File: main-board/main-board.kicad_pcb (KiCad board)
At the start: 4 copper layers, 142.9 x 86.4 mm, 168 parts, among them J1 BOOT, J10 8P8CDouble, J11 Qwiic, J12 Qwiic, J13 Qwiic, J14 EthernetLEDs, J2 USB Header, J3 JTAG, J4 5V Input, J5 StatusPanel, J6 Magjack, J7 8P8CDouble, J8 8P8CDouble, J9 8P8CDouble, Q1 N Channel, Q10 N Channel, Q11 N Channel, Q12 N Channel, Q13 P Channel, Q14 P Channel, Q15 P Channel, Q16 P Channel, Q17 P Channel, Q2 N Channel, Q3 N Channel, Q4 N Channel, Q5 P Channel, Q6 P Channel, Q7 P Channel, Q8 P Channel, Q9 N Channel, U1 STM32H743ZITx, U10 ISL83490, U11 ISL83490, U12 ISL83490, U13 W25Q80DVSNIG, U2 USBLC6-2SC6, U3 3.3V Reg, U4 KSZ8041MLL, U5 ISL83490, U6 ISL83490, U7 ISL83490, U8 ISL83490, U9 ISL83490, X1 20MHz Oscillator, X2 25MHz Oscillator

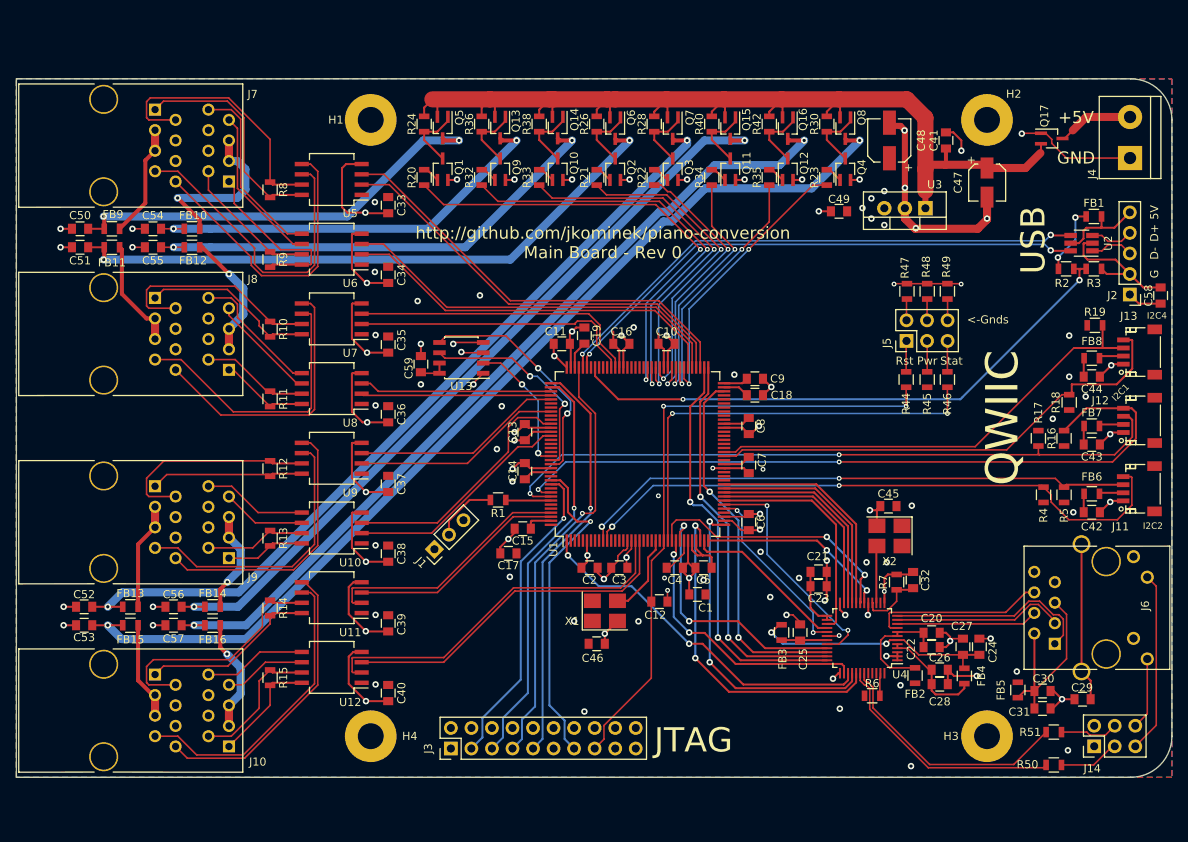
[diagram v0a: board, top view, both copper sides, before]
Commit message: First round of rev 1 changes. This was a complete relayout.
* RS485 transceiver footprint fixed
* Compressed board to 100x100mm exactly
* Removed ethernet
* Changed FET footprints to SOT-23
* Swapped USB D+/D- to correct positions
* Spaced out +5V and GND silkscreen on power input
* Added JLCPCB order number silkscreen
* Spaced out Qwiic headers
* Added some more space around 3.3V regulator.
* Slightly increased size of electrolytic caps.
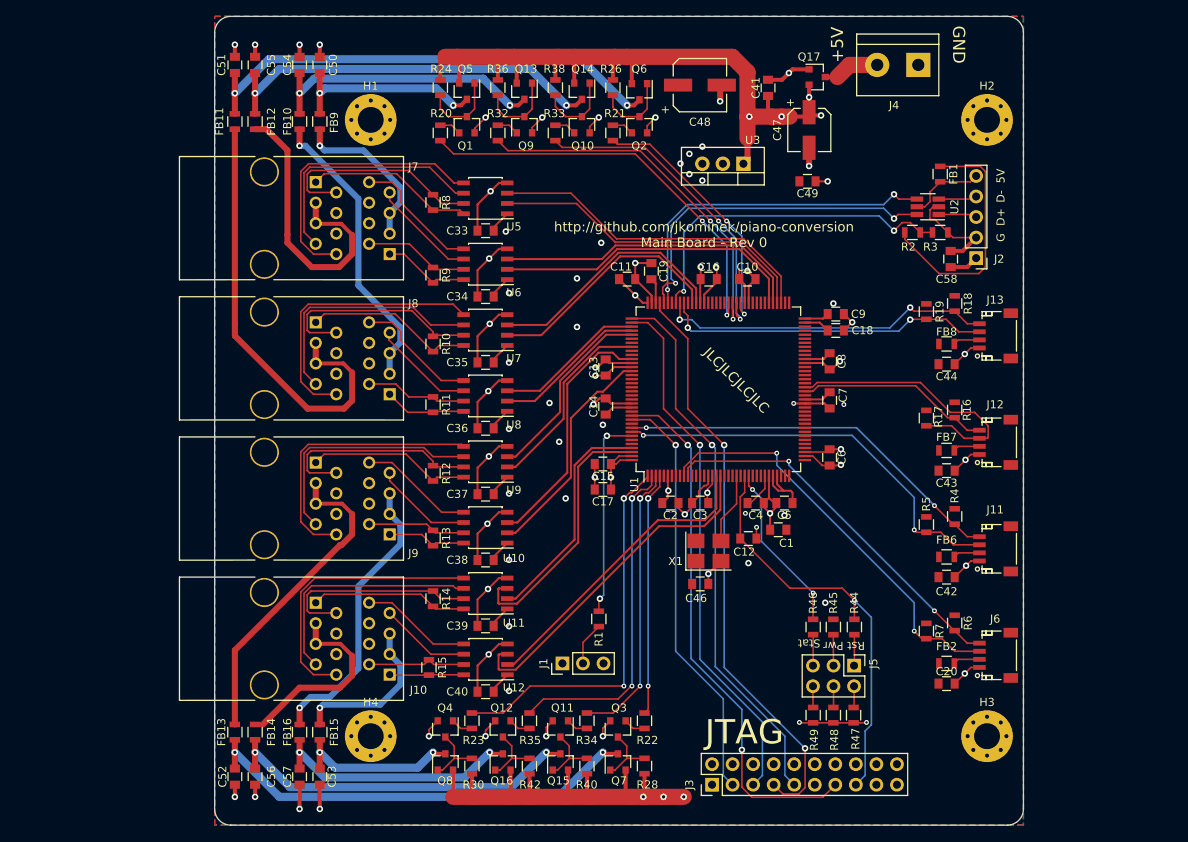
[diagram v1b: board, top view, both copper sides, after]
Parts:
- removed C21: 22uF, Capacitors_SMD:C_0805
- removed C22, C23, C25, C26, C27, C28, C29, C30, C31, C32: 0.1uF, Capacitors_SMD:C_0805
- removed C24: 1uF, Capacitors_SMD:C_0805
- removed C45: DC, Capacitors_SMD:C_0805
- removed C59: DC6, Capacitors_SMD:C_0805
- removed FB3, FB4, FB5: FB, Inductors_SMD:L_0805
- removed J14: EthernetLEDs, Pin_Headers:Pin_Header_Straight_2x03_Pitch2.54mm
- removed R50, R51: 330, Resistors_SMD:R_0805
- removed U13: W25Q80DVSNIG, Housings_SOIC:SOIC-8_3.9x4.9mm_Pitch1.27mm
- removed U4: KSZ8041MLL, Housings_QFP:LQFP-48_7x7mm_Pitch0.5mm
- removed X2: 25MHz Oscillator, Oscillators:Oscillator_SMD_SeikoEpson_SG8002CE-4pin_3.2x2.5mm_HandSoldering
- C20: value 22uF -> 1uF
- C47: footprint Capacitors_SMD:CP_Elec_4x4.5 -> Capacitors_SMD:CP_Elec_5x5.3
- C48: footprint Capacitors_SMD:CP_Elec_5x5.3 -> Capacitors_SMD:CP_Elec_6.3x5.8
- H1, H2, H3, H4: footprint Mounting_Holes:MountingHole_3.2mm_M3_Pad -> Mounting_Holes:MountingHole_3.2mm_M3_Pad_Via
- J6: value Magjack -> Qwiic; footprint footprints:J1B1211111CCD -> Connectors_JST:JST_SH_SM04B-SRSS-TB_04x1.00mm_Angled
- Q1, Q10, Q11, Q12, Q13, Q14, Q15, Q16, Q17, Q2, Q3, Q4, Q5, Q6, Q7, Q8, Q9: footprint TO_SOT_Packages_SMD:SOT-323_SC-70_Handsoldering -> TO_SOT_Packages_SMD:SOT-23
- R6: value 0 -> 1200
- R7: value 6490 -> 1200
- U10, U11, U12, U5, U6, U7, U8, U9: footprint Housings_SOIC:SO-8_5.3x6.2mm_Pitch1.27mm -> Housings_SOIC:SOIC-8_3.9x4.9mm_Pitch1.27mm
- moved Q8 92.7 mm to (123.5, 130.2), turned to 90 degrees
- moved R30 90.7 mm to (126.8, 130.7), turned to 90 degrees
- moved Q16 85.9 mm to (130.6, 130.2), turned to 90 degrees
- moved Q4 85.1 mm to (123.5, 126.1), turned to 270 degrees
- moved R42 84.7 mm to (133.9, 130.7), turned to 90 degrees
- moved Q15 81.1 mm to (137.8, 130.2), turned to 90 degrees
- moved R40 80.9 mm to (141.0, 130.7), turned to 90 degrees
- moved R23 80.2 mm to (126.8, 125.1), turned to 90 degrees
- moved R28 79.4 mm to (148.1, 130.7), turned to 90 degrees
- moved Q7 78.7 mm to (144.9, 130.2), turned to 90 degrees
- moved Q12 77.7 mm to (130.6, 126.1), turned to 270 degrees
- moved R35 73.4 mm to (133.9, 125.1), turned to 90 degrees
- moved Q11 72.3 mm to (137.8, 126.1), turned to 270 degrees
- moved Q3 69.5 mm to (144.9, 126.1), turned to 270 degrees
- moved R34 68.9 mm to (141.0, 125.1), turned to 90 degrees
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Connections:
- C20 pad 1: GND -> +3V3
- C20 pad 2: Net-(C20-Pad2) -> GND
- FB10 pad 1: PWR2 -> PWR4
- FB12 pad 1: PWR4 -> PWR1
- FB14 pad 1: PWR6 -> PWR7
- FB15 pad 1: PWR7 -> PWR8
- FB16 pad 1: PWR8 -> PWR6
- FB2 pad 1: Net-(C20-Pad2) -> +3V3
- FB2 pad 2: +3V3 -> Net-(FB2-Pad2)
- FB9 pad 1: PWR1 -> PWR2
- J11 pad 3: /I2C2_SDA -> /I2C1_SDA
- J11 pad 4: /I2C2_SCL -> /I2C1_SCL
- J12 pad 3: /I2C1_SDA -> /I2C4_SDA
- J12 pad 4: /I2C1_SCL -> /I2C4_SCL
- J13 pad 3: /I2C4_SDA -> /I2C3_SDA
- J13 pad 4: /I2C4_SCL -> /I2C3_SCL
- J2 pad 3: /D- -> /D+
- J2 pad 4: /D+ -> /D-
- J6 pad 1: /ETH_TD+ -> GND
- J6 pad 2: Net-(C30-Pad1) -> Net-(FB2-Pad2)
- J6 pad 3: /ETH_TD- -> /I2C2_SDA
- J6 pad 4: /ETH_RD+ -> /I2C2_SCL
- R16 pad 2: /I2C1_SCL -> /I2C4_SCL
- R17 pad 2: /I2C1_SDA -> /I2C4_SDA
- R18 pad 2: /I2C4_SCL -> /I2C3_SCL
- R19 pad 2: /I2C4_SDA -> /I2C3_SDA
- R20 pad 2: /PWR1_CTRL -> /PWR2_CTRL
- R23 pad 2: /PWR7_CTRL -> /PWR8_CTRL
- R32 pad 2: /PWR2_CTRL -> /PWR4_CTRL
- R33 pad 2: /PWR4_CTRL -> /PWR1_CTRL
- R34 pad 2: /PWR6_CTRL -> /PWR7_CTRL
- R35 pad 2: /PWR8_CTRL -> /PWR6_CTRL
- R4 pad 2: /I2C2_SCL -> /I2C1_SCL
- R5 pad 2: /I2C2_SDA -> /I2C1_SDA
- R6 pad 1: Net-(R6-Pad1) -> +3V3
- R6 pad 2: +3V3 -> /I2C2_SCL
- R7 pad 1: Net-(C32-Pad1) -> +3V3
- R7 pad 2: GND -> /I2C2_SDA
- U1 pad 1: /ETH_TXD3 -> /PWR8_CTRL
- U1 pad 100: (no net) -> /I2C3_SCL
- U1 pad 127: /SPI6_MISO -> (no net)
- U1 pad 128: /SPI6_SCK -> (no net)
- U1 pad 129: /SPI6_MOSI -> (no net)
- U1 pad 2: (no net) -> /PWR6_CTRL
- U1 pad 27: /ETH_MDC -> (no net)
- U1 pad 28: /ETH_TXD2 -> (no net)
- U1 pad 29: /ETH_TX_CLK -> (no net)
- U1 pad 3: (no net) -> /PWR7_CTRL
- U1 pad 34: /ETH_CRS -> (no net)
- U1 pad 35: /ETH_RX_CLK -> (no net)
- U1 pad 36: /ETH_MDIO -> (no net)
- U1 pad 37: /ETH_COL -> (no net)
- U1 pad 4: (no net) -> /PWR5_CTRL
- U1 pad 41: /ETH_RXER -> (no net)
- U1 pad 42: /ETH_INTRP -> (no net)
- U1 pad 43: /ETH_RX_DV -> (no net)
- U1 pad 44: /ETH_RXD0 -> (no net)
- U1 pad 45: /ETH_RXD1 -> (no net)
- U1 pad 46: /ETH_RXD2 -> (no net)
- U1 pad 47: /ETH_RXD3 -> (no net)
- U1 pad 70: /ETH_TX_EN -> (no net)
- U1 pad 73: /ETH_TXD0 -> (no net)
- U1 pad 74: /ETH_TXD1 -> (no net)
- U1 pad 79: /PWR7_CTRL -> (no net)
- U1 pad 80: /PWR8_CTRL -> (no net)
- U1 pad 81: /PWR6_CTRL -> (no net)
- U1 pad 82: /PWR5_CTRL -> (no net)
- U1 pad 86: /PWR4_CTRL -> /PWR1_CTRL
- U1 pad 87: /PWR2_CTRL -> /PWR4_CTRL
- U1 pad 88: /PWR1_CTRL -> /PWR2_CTRL
- U1 pad 99: (no net) -> /I2C3_SDA
- U2 pad 1: /D- -> /D+
- U2 pad 3: /D+ -> /D-
- U2 pad 4: /USB_D+ -> /USB_D-
- U2 pad 6: /USB_D- -> /USB_D+
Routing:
- net Net-(C53-Pad1): track 124.8 -> 20.7 mm
- net GND: track 316.2 -> 219.3 mm, vias 68 -> 48
- net Net-(C57-Pad1): track 105.3 -> 31.3 mm
- net Net-(C56-Pad1): track 96.7 -> 44.9 mm
- net /ETH_TXD1: track 50.8 -> 0.00 mm, vias 2 -> 0
- net /ETH_TXD0: track 48.5 -> 0.00 mm, vias 2 -> 0
- net Net-(C52-Pad1): track 101.4 -> 55.5 mm
- net /ETH_TX_EN: track 45.6 -> 0.00 mm, vias 2 -> 0
- net /ETH_TXD3: track 44.2 -> 0.00 mm, vias 2 -> 0
- net /I2C1_SCL: track 91.8 -> 48.6 mm
- net /ETH_CRS: track 41.7 -> 0.00 mm, vias 2 -> 0
- net /I2C3_SCL: track 0.00 -> 41.5 mm, vias 0 -> 2
- net PWR3: track 13.8 -> 55.2 mm
- net /I2C3_SDA: track 0.00 -> 40.8 mm, vias 0 -> 2
- net /ETH_COL: track 39.6 -> 0.00 mm, vias 2 -> 0
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- added copper zone on In2.Cu, net +5V
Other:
- board size 142.9 x 86.4 mm -> 100 x 100 mm
- board text added: "JLCJLCJLCJLC"
- board text removed: "<-Gnds"
- board text removed: "I2C1"
- board text removed: "I2C2"
- board text removed: "I2C4"
- board text removed: "QWIIC"
- board text removed: "USB"

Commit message: MicroSD card slot and some IRQ headers.
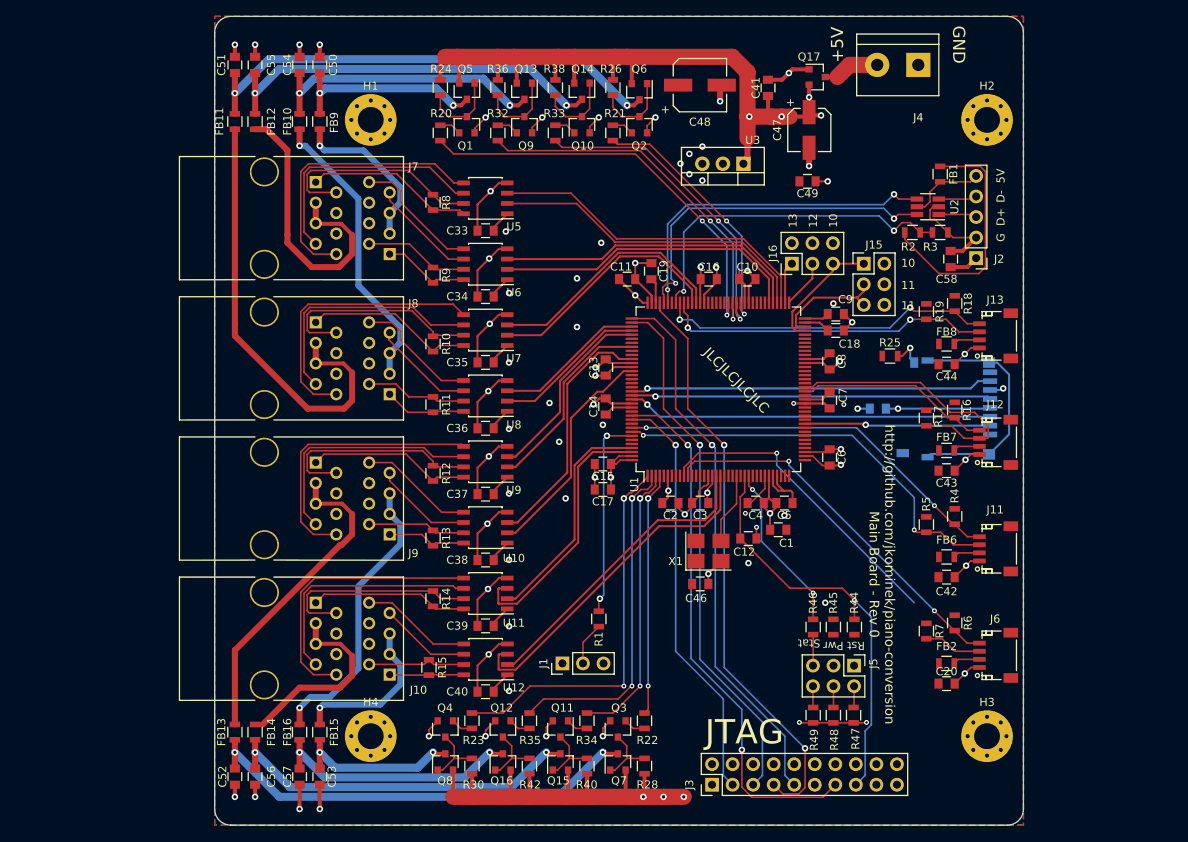
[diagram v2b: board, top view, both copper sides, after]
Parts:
- added C21: DC, Capacitors_SMD:C_0805, B.Cu at (177.0, 86.5)
- added J14: Micro_SD_Card_Det, footprints:114-00841-68, B.Cu at (190.0, 82.0)
- added J15: Interrupts1, Pin_Headers:Pin_Header_Straight_2x03_Pitch2.54mm, F.Cu at (175.3, 68.6)
- added J16: Interrupts2, Pin_Headers:Pin_Header_Straight_2x03_Pitch2.54mm, F.Cu at (166.4, 68.6)
- added R25: 10k, Resistors_SMD:R_0805, F.Cu at (178.5, 80.0)
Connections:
- U1 pad 127: (no net) -> /SPI6_MISO
- U1 pad 128: (no net) -> /SPI6_SCK
- U1 pad 129: (no net) -> /SPI6_MOSI
- U1 pad 46: (no net) -> /SDCARD_CS
- U1 pad 66: (no net) -> GND
- U1 pad 69: (no net) -> /QWIIC_EXTI10
- U1 pad 70: (no net) -> /QWIIC_EXTI11
- U1 pad 73: (no net) -> /QWIIC_EXTI12
- U1 pad 74: (no net) -> /QWIIC_EXTI13
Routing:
- net /SPI6_MOSI: track 0.00 -> 45.2 mm, vias 0 -> 1
- net /SPI6_MISO: track 0.00 -> 44.8 mm, vias 0 -> 1
- net /SPI6_SCK: track 0.00 -> 44.5 mm, vias 0 -> 1
- net Net-(J14-Pad11): track 0.00 -> 29.5 mm
- net /SDCARD_CS: track 0.00 -> 23.0 mm, vias 0 -> 1
- net /QWIIC_EXTI10: track 0.00 -> 15.5 mm
- net /QWIIC_EXTI11: track 0.00 -> 14.2 mm
- net +3V3: track 87.6 -> 100.5 mm, vias 33 -> 34
- net /QWIIC_EXTI12: track 0.00 -> 6.02 mm
- net /QWIIC_EXTI13: track 0.00 -> 5.18 mm
- net /I2C2_SDA: track 51.4 -> 46.5 mm, vias 2 -> 1
- net Net-(J14-Pad9): track 0.00 -> 3.97 mm, vias 0 -> 1
- net Net-(J5-Pad1): track 3.84 -> 0.00 mm
- net Net-(J5-Pad3): track 3.83 -> 0.00 mm
- net GND: track 219.3 -> 222.5 mm, vias 48 -> 50
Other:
- board text added: "10"
- board text added: "11"
- board text added: "12"
- board text added: "13"

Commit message: Add RTC oscillator, battery header and LDO
Also moved the boot pin to defaulting from flash.
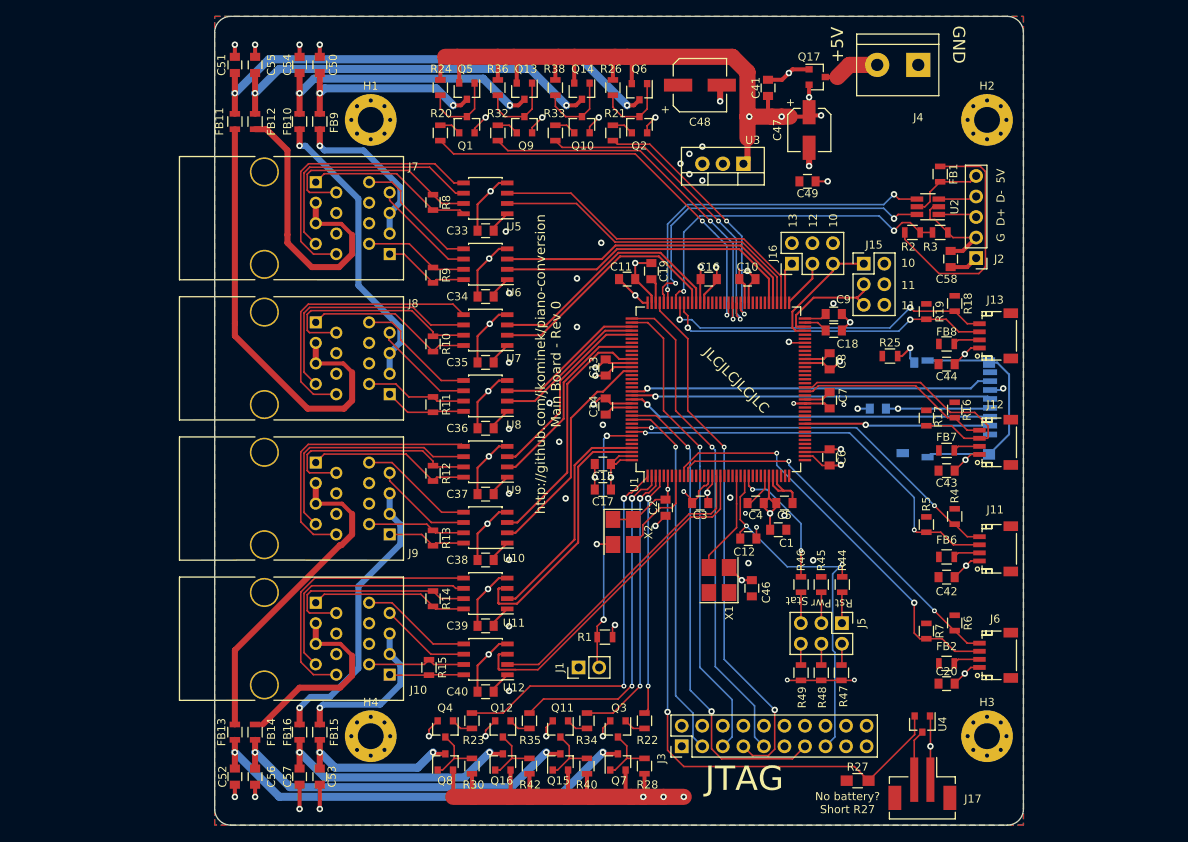
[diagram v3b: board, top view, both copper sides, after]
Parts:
- added J17: Battery, Connectors_JST:JST_PH_B2B-PH-SM4-TB_02x2.00mm_Straight, F.Cu at (182.5, 133.5)
- added R27: DNP, Resistors_SMD:R_0805_HandSoldering, F.Cu at (174.5, 132.5)
- added U4: AP2120N-3.3TRG1 / XC6206P332MR, TO_SOT_Packages_SMD:SOT-23, F.Cu at (182.5, 125.5)
- added X2: 32.768kHz Oscillator, Oscillators:Oscillator_SMD_SeikoEpson_SG8002CE-4pin_3.2x2.5mm_HandSoldering, F.Cu at (145.5, 101.8)
- J1: footprint Pin_Headers:Pin_Header_Straight_1x03_Pitch2.54mm -> Pin_Headers:Pin_Header_Straight_1x02_Pitch2.54mm
- moved C46 6.40 mm to (161.4, 108.7), turned to 90 degrees
- moved J3 6.05 mm to (152.8, 128.2)
- moved J5 5.46 mm to (172.6, 113.0)
- moved R44 5.46 mm to (172.6, 108.2)
- moved R45 5.46 mm to (170.0, 108.2)
- moved R46 5.46 mm to (167.5, 108.2)
- moved R47 5.46 mm to (172.5, 119.2)
- moved R48 5.46 mm to (170.0, 119.2)
- moved R49 5.46 mm to (167.5, 119.2)
- moved X1 3.82 mm to (157.4, 107.7), turned to 90 degrees
- moved R1 2.37 mm to (143.2, 114.8), turned to 180 degrees
- moved J1 2.06 mm to (140.0, 118.5)
- moved C2 0.83 mm to (150.8, 98.8), turned to 270 degrees
- moved C18 0.25 mm to (171.5, 76.8)
- moved C9 0.25 mm to (171.5, 74.8)
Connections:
- net Net-(U1-Pad23) renamed /HSE_OSC
- C2 pad 1: +3V3 -> +BATT
- R1 pad 1: Net-(R1-Pad1) -> GND
- U1 pad 138: Net-(R1-Pad1) -> Net-(J1-Pad2)
- U1 pad 6: +3V3 -> +BATT
- U1 pad 8: (no net) -> /LSE_OSC
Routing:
- net +BATT: track 0.00 -> 79.6 mm, vias 0 -> 2
- net Net-(J1-Pad2): track 5.36 -> 32.3 mm, vias 0 -> 2
- net Net-(R1-Pad1): track 25.2 -> 0.00 mm, vias 2 -> 0
- net GND: track 222.5 -> 236.7 mm, vias 50 -> 55
- net /LSE_OSC: track 0.00 -> 11.5 mm
- net /JTDO: track 66.2 -> 59.8 mm
- net /JTMS: track 72.1 -> 65.8 mm
- net /JTDI: track 65.5 -> 59.2 mm
- net /JTCK: track 67.6 -> 61.3 mm
- net Net-(J17-Pad2): track 0.00 -> 6.29 mm
- net /JNTRST: track 51.6 -> 45.3 mm
- net /I2C2_SDA: track 46.5 -> 52.1 mm, vias 1 -> 2
- net /LEDSTATUS: track 21.0 -> 16.2 mm
- net /NRST: track 52.1 -> 47.8 mm, vias 1 -> 2
- net /HSE_OSC: track 8.84 -> 12.8 mm
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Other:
- board text added: "No battery? Short R27"

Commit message: Tweak a bunch of traces, bump the board rev
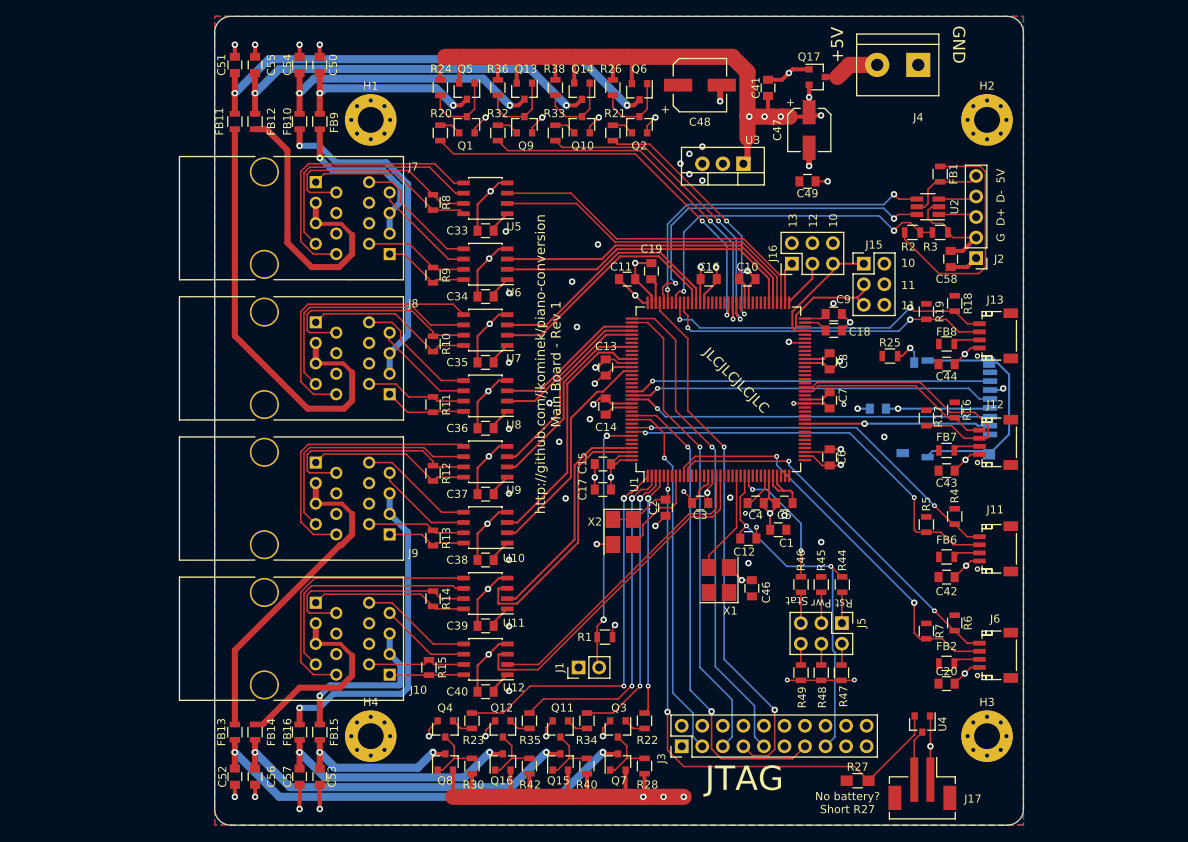
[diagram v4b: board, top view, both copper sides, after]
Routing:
- net PWR6: track 35.7 -> 41.5 mm
- net PWR4: track 36.4 -> 41.8 mm
- net /NRST: track 47.8 -> 46.0 mm
- net PWR8: track 20.1 -> 20.9 mm
- net PWR2: track 20.4 -> 21.3 mm
- net /SPI6_SCK: track 44.5 -> 45.2 mm
- net GND: track 236.7 -> 237.4 mm, vias 55 -> 56
- net /I2C2_SDA: track 52.1 -> 51.5 mm
- net +3V3: track 96.6 -> 97.1 mm
- net +5V: vias 7 -> 8
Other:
- board text added: "http://github.com/jkominek/piano-conversion Main Board - Rev 1"
- board text removed: "http://github.com/jkominek/piano-conversion Main Board - Rev 0"
